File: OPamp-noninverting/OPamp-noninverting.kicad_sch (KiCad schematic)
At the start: 6 parts, among them U1 ${SIM.PARAMS}

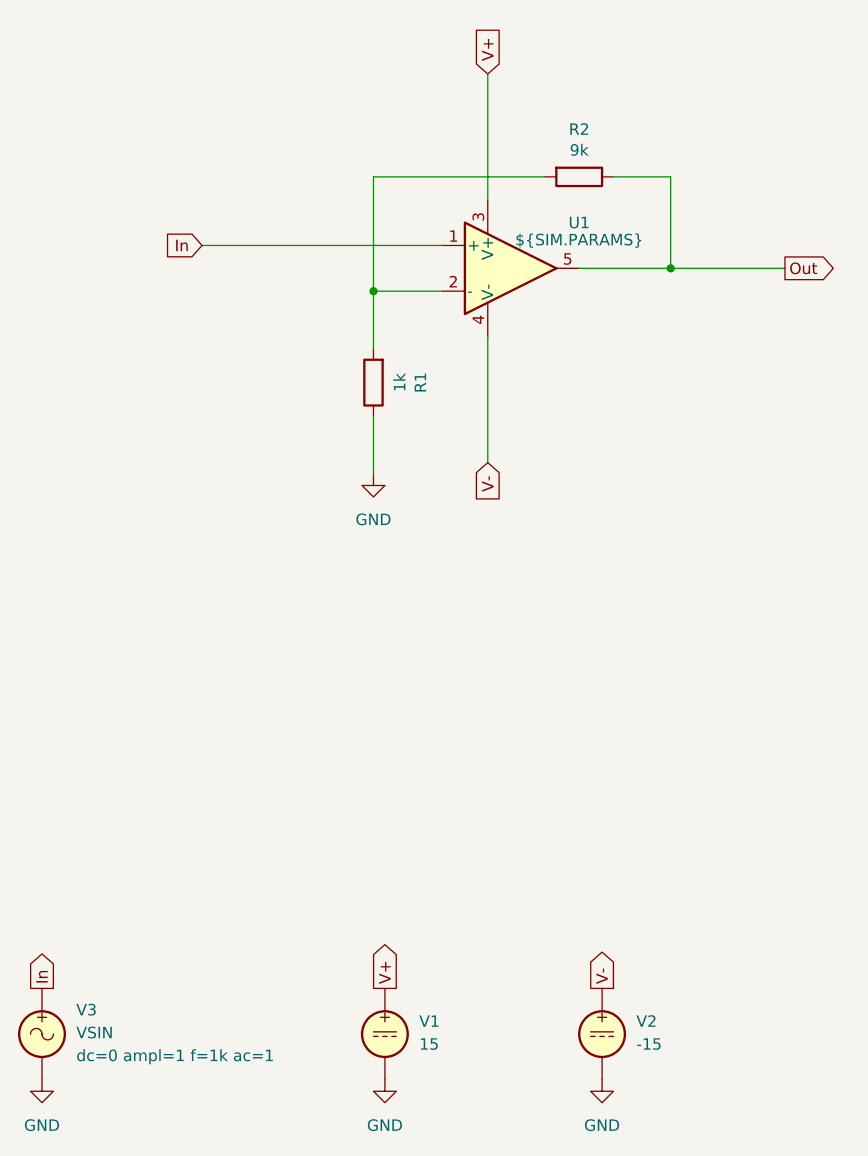
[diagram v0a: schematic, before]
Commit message: Tested/updated for KiCad 9
Schematics are tested and updated for KiCad 9, no changes in circuitry
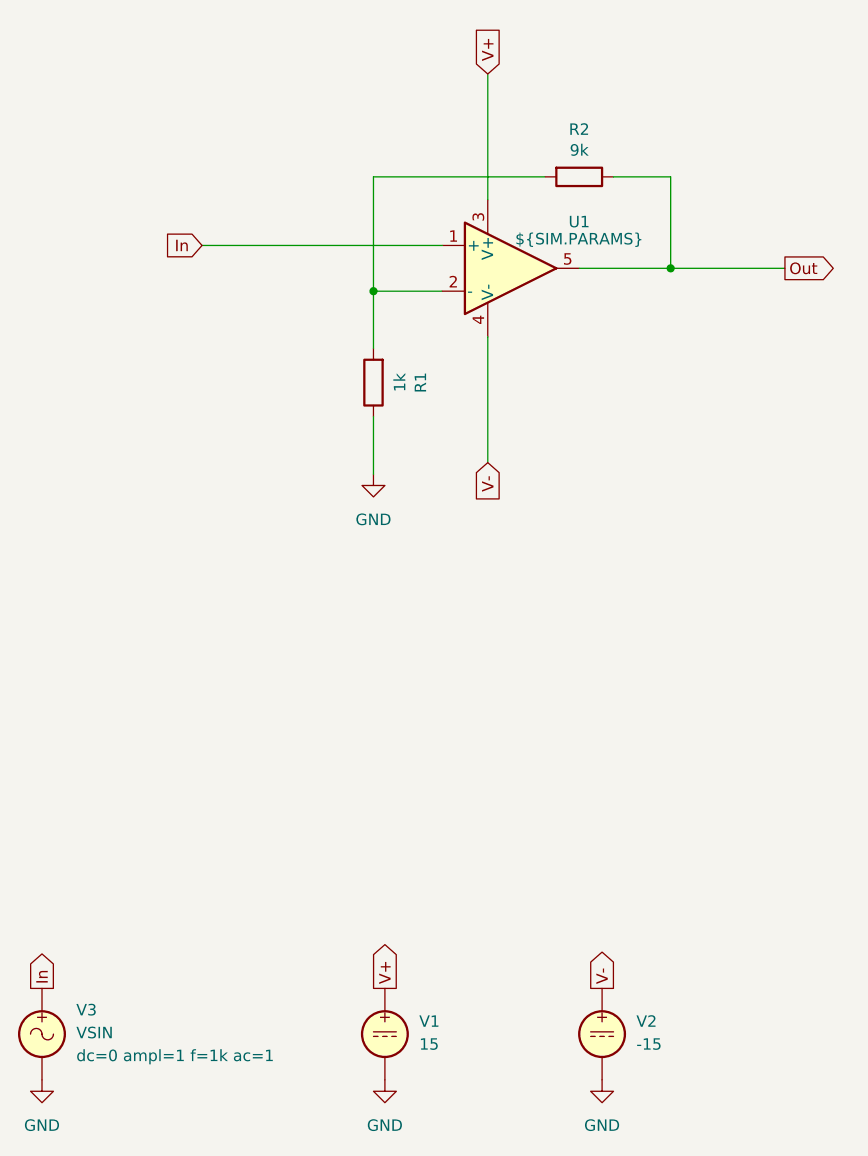
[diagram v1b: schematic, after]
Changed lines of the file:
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@@
 (kicad_sch
-	(version 20231120)
+	(version 20250114)
 	(generator "eeschema")
-	(generator_version "8.0")
+	(generator_version "9.0")
 	(paper "A4")
 	(title_block
 		(title "OPamp, noninverting")
-		(date "2024-12-15")
+		(date "2025-09-13")
 		(company "GitHub/OJStuff")
 	)
@@
 		(fields_autoplaced yes)
 		(property "Reference" "U1"
-			(at 157.48 91.4714 0)
+			(at 157.48 91.3698 0)
 			(effects
 				(font
@@
 		)
 		(property "Value" "${SIM.PARAMS}"
-			(at 157.48 93.3765 0)
+			(at 157.48 93.2749 0)
 			(effects
 				(font
@@
 			)
 		)
-		(property "Description" "Operational amplifier, single, node sequence=1:+ 2:- 3:OUT 4:V+ 5:V-"
+		(property "Description" "Operational amplifier, single"
 			(at 149.86 96.52 0)
 			(effects
@@
 			)
 		)
-		(property "Sim.Library" "${KICAD7_SYMBOL_DIR}/Simulation_SPICE.sp"
+		(property "Sim.Library" "${KICAD9_SYMBOL_DIR}/Simulation_SPICE.sp"
 			(at 149.86 96.52 0)
 			(effects
@@
 			)
 		)
+		(pin "2"
+		)
+		(pin "5"
+		)
+		(pin "3"
+		)
 		(pin "4"
 		)
 		(pin "1"
 		)
-		(pin "5"
-		)
-		(pin "3"
-		)
-		(pin "2"
-		)
 		(instances
-			(project "OPamp-noninverting-(.tran)"
+			(project ""
 				(path "/a81f47c8-d758-4a1a-b078-3bf1b27e0f5d"
 					(reference "U1")
@@
 		)
 	)
+	(embedded_fonts no)
 )
